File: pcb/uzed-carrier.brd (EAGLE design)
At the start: 51.2 x 43.2 mm, 16 parts

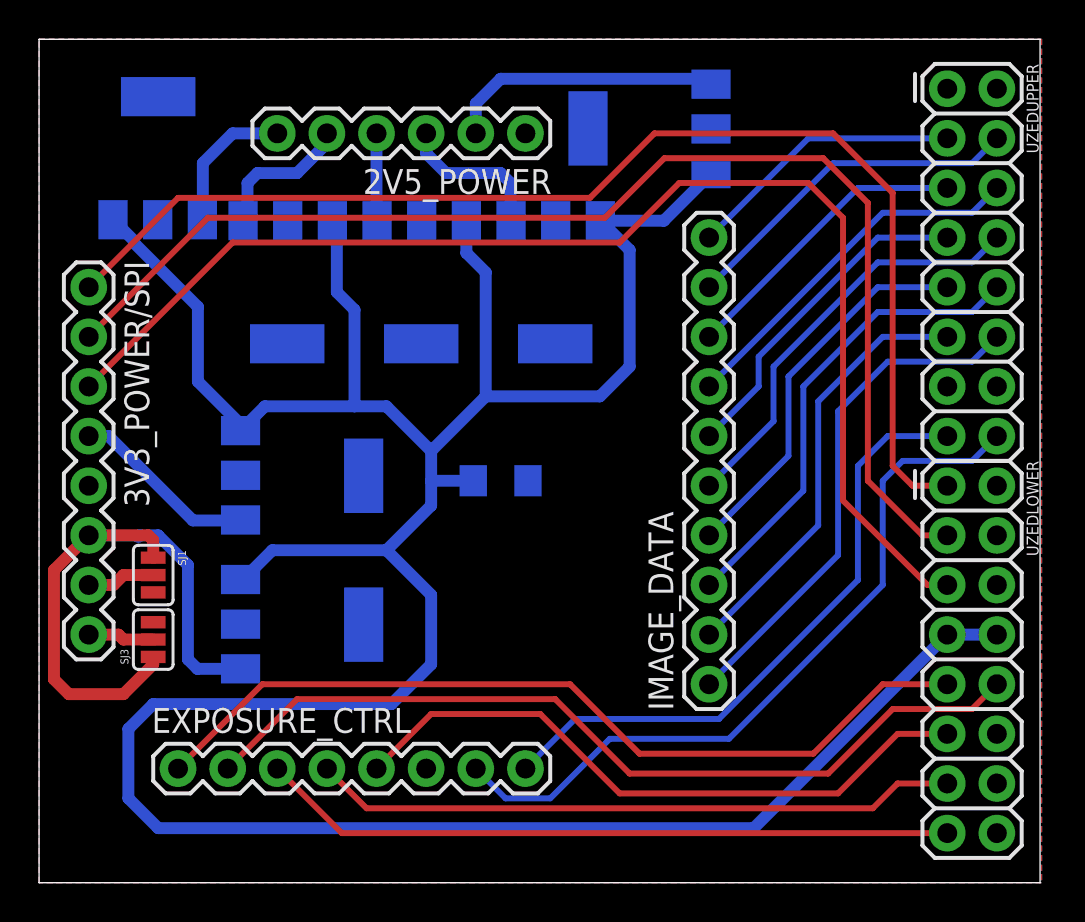
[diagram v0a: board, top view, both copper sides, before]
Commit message: added mosfet for fpga control of board power
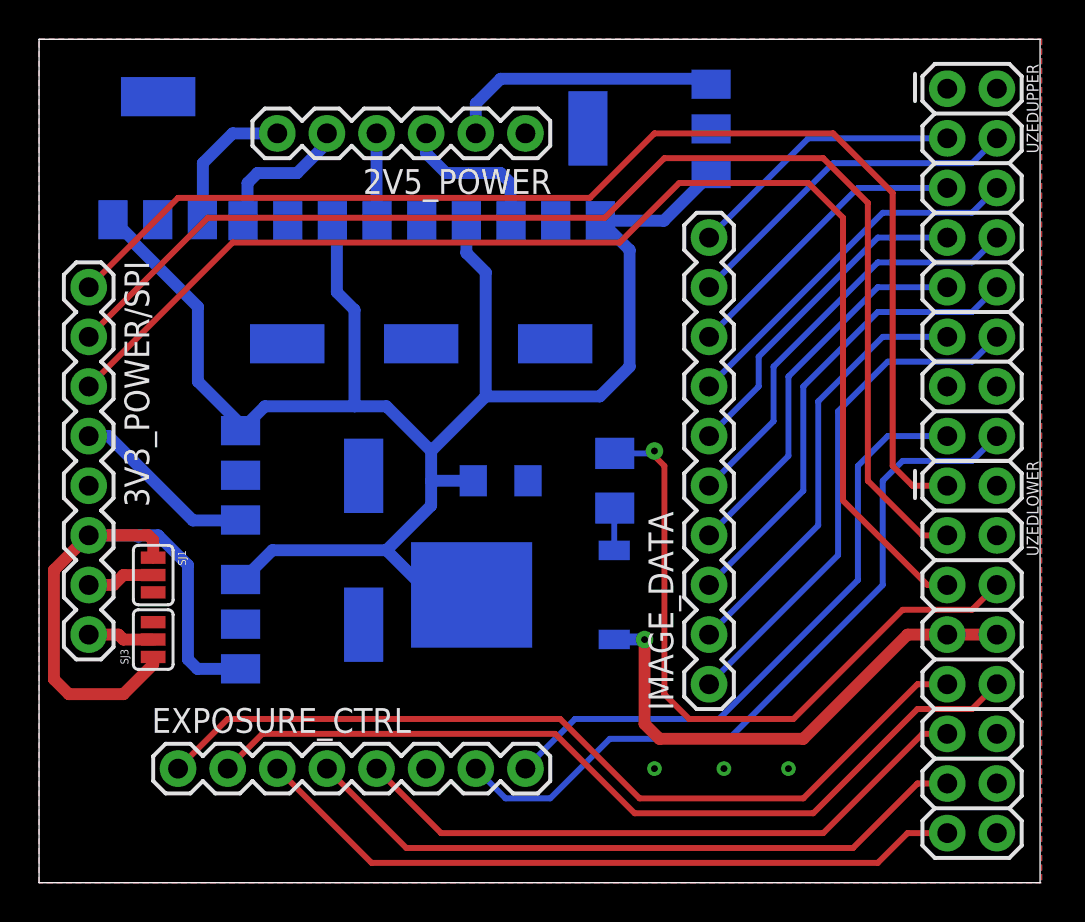
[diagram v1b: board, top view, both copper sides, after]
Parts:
- added Q1: IRFR5305, transistor-power:D-PAK_TO252AA
- added R1: (no value), rcl:M1206
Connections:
- new net FET_GATE: Q1.1, R1.2
- new net N$1: R1.1, UZEDLOWER.6
- new net VRAW: Q1.3, UZEDLOWER.7, UZEDLOWER.8
- net VIN: now also Q1.4; no longer UZEDLOWER.7, UZEDLOWER.8
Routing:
- net VIN: track 163.4 -> 92.4 mm
- net N$1: track 0.00 -> 35.1 mm, vias 0 -> 1
- net VRAW: track 0.00 -> 26.4 mm, vias 0 -> 1
- net FET_GATE: track 0.00 -> 2.17 mm
- net INT_TIME2: track 33.1 -> 34.8 mm
- net INT_TIME3: track 35.7 -> 36.9 mm
- net INT_TIME1: track 33.3 -> 32.7 mm
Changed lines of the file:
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@@
 <attribute name="PROD_ID" value="CAP-00811" x="23.622" y="20.574" size="1.778" layer="28" rot="MR0" display="off"/>
 </element>
+<element name="Q1" library="transistor-power" library_urn="urn:adsk.eagle:library:400" package="D-PAK_TO252AA" package3d_urn="urn:adsk.eagle:package:29503/1" value="IRFR5305" x="24.638" y="14.732" rot="MR270"/>
+<element name="R1" library="rcl" library_urn="urn:adsk.eagle:library:334" package="M1206" package3d_urn="urn:adsk.eagle:package:23566/1" value="" x="29.464" y="20.574" rot="MR270"/>
 </elements>
 <signals>
@@
 <contactref element="SJ3" pad="3"/>
 <contactref element="C1" pad="-"/>
+<via x="31.496" y="5.842" extent="1-16" drill="0.35"/>
+<via x="35.052" y="5.842" extent="1-16" drill="0.35"/>
+<via x="38.354" y="5.842" extent="1-16" drill="0.35"/>
 </signal>
 <signal name="VIN">
@@
 <contactref element="3V3_4" pad="3"/>
 <contactref element="3V3_3" pad="3"/>
-<contactref element="UZEDLOWER" pad="7"/>
-<contactref element="UZEDLOWER" pad="8"/>
-<wire x1="49.022" y1="12.7" x2="46.482" y2="12.7" width="0.6096" layer="16"/>
-<wire x1="46.482" y1="12.7" x2="36.576" y2="2.794" width="0.6096" layer="16"/>
-<wire x1="36.576" y1="2.794" x2="6.096" y2="2.794" width="0.6096" layer="16"/>
-<wire x1="6.096" y1="2.794" x2="4.572" y2="4.318" width="0.6096" layer="16"/>
-<wire x1="4.572" y1="4.318" x2="4.572" y2="7.874" width="0.6096" layer="16"/>
-<wire x1="4.572" y1="7.874" x2="5.842" y2="9.144" width="0.6096" layer="16"/>
-<wire x1="5.842" y1="9.144" x2="18.034" y2="9.144" width="0.6096" layer="16"/>
-<wire x1="18.034" y1="9.144" x2="20.066" y2="11.176" width="0.6096" layer="16"/>
-<wire x1="20.066" y1="14.732" x2="20.066" y2="11.176" width="0.6096" layer="16"/>
-<wire x1="11.938" y1="17.018" x2="17.78" y2="17.018" width="0.6096" layer="16"/>
+<wire x1="17.78" y1="17.018" x2="11.938" y2="17.018" width="0.6096" layer="16"/>
 <wire x1="11.938" y1="17.018" x2="10.4394" y2="15.5194" width="0.6096" layer="16"/>
 <wire x1="10.4394" y1="15.5194" x2="10.3124" y2="15.5194" width="0.6096" layer="16"/>
@@
 <wire x1="8.128" y1="25.654" x2="10.3124" y2="23.4696" width="0.6096" layer="16"/>
 <wire x1="10.3124" y1="23.4696" x2="10.3124" y2="23.1394" width="0.6096" layer="16"/>
-<wire x1="17.78" y1="17.018" x2="20.066" y2="14.732" width="0.6096" layer="16"/>
 <contactref element="C1" pad="+"/>
 <wire x1="22.222" y1="20.574" x2="20.06829375" y2="20.574" width="0.6096" layer="16"/>
 <wire x1="20.06829375" y1="20.574" x2="20.066" y2="20.57629375" width="0.6096" layer="16"/>
+<contactref element="Q1" pad="4"/>
+<wire x1="22.138" y1="14.732" x2="20.066" y2="14.732" width="0.6096" layer="16"/>
+<wire x1="20.066" y1="14.732" x2="17.78" y2="17.018" width="0.6096" layer="16"/>
 </signal>
 <signal name="D0">
@@
 <contactref element="EXPOSURE_CTRL" pad="5"/>
 <contactref element="UZEDLOWER" pad="11"/>
-<wire x1="17.272" y1="5.842" x2="20.066" y2="8.636" width="0.3048" layer="1"/>
-<wire x1="20.066" y1="8.636" x2="25.654" y2="8.636" width="0.3048" layer="1"/>
-<wire x1="25.654" y1="8.636" x2="29.718" y2="4.572" width="0.3048" layer="1"/>
-<wire x1="40.894" y1="4.572" x2="43.942" y2="7.62" width="0.3048" layer="1"/>
-<wire x1="43.942" y1="7.62" x2="46.482" y2="7.62" width="0.3048" layer="1"/>
-<wire x1="29.718" y1="4.572" x2="40.894" y2="4.572" width="0.3048" layer="1"/>
+<wire x1="17.272" y1="5.842" x2="20.574" y2="2.54" width="0.3048" layer="1"/>
+<wire x1="40.132" y1="2.54" x2="45.212" y2="7.62" width="0.3048" layer="1"/>
+<wire x1="45.212" y1="7.62" x2="46.482" y2="7.62" width="0.3048" layer="1"/>
+<wire x1="20.574" y1="2.54" x2="40.132" y2="2.54" width="0.3048" layer="1"/>
 </signal>
 <signal name="INT_TIME2">
 <contactref element="EXPOSURE_CTRL" pad="4"/>
 <contactref element="UZEDLOWER" pad="13"/>
-<wire x1="14.732" y1="5.842" x2="16.764" y2="3.81" width="0.3048" layer="1"/>
-<wire x1="16.764" y1="3.81" x2="42.672" y2="3.81" width="0.3048" layer="1"/>
-<wire x1="42.672" y1="3.81" x2="43.942" y2="5.08" width="0.3048" layer="1"/>
-<wire x1="43.942" y1="5.08" x2="46.482" y2="5.08" width="0.3048" layer="1"/>
+<wire x1="14.732" y1="5.842" x2="18.796" y2="1.778" width="0.3048" layer="1"/>
+<wire x1="18.796" y1="1.778" x2="41.656" y2="1.778" width="0.3048" layer="1"/>
+<wire x1="41.656" y1="1.778" x2="44.958" y2="5.08" width="0.3048" layer="1"/>
+<wire x1="44.958" y1="5.08" x2="46.482" y2="5.08" width="0.3048" layer="1"/>
 </signal>
 <signal name="INT_TIME3">
 <contactref element="EXPOSURE_CTRL" pad="3"/>
 <contactref element="UZEDLOWER" pad="15"/>
-<wire x1="12.192" y1="5.842" x2="15.494" y2="2.54" width="0.3048" layer="1"/>
-<wire x1="15.494" y1="2.54" x2="46.482" y2="2.54" width="0.3048" layer="1"/>
+<wire x1="12.192" y1="5.842" x2="17.018" y2="1.016" width="0.3048" layer="1"/>
+<wire x1="17.018" y1="1.016" x2="42.926" y2="1.016" width="0.3048" layer="1"/>
+<wire x1="42.926" y1="1.016" x2="44.45" y2="2.54" width="0.3048" layer="1"/>
+<wire x1="44.45" y1="2.54" x2="46.482" y2="2.54" width="0.3048" layer="1"/>
 </signal>
 <signal name="FRAME_VALID">
 <contactref element="EXPOSURE_CTRL" pad="2"/>
 <contactref element="UZEDLOWER" pad="10"/>
-<wire x1="9.652" y1="5.842" x2="13.208" y2="9.398" width="0.3048" layer="1"/>
-<wire x1="26.416" y1="9.398" x2="30.226" y2="5.588" width="0.3048" layer="1"/>
-<wire x1="30.226" y1="5.588" x2="40.386" y2="5.588" width="0.3048" layer="1"/>
-<wire x1="40.386" y1="5.588" x2="43.688" y2="8.89" width="0.3048" layer="1"/>
-<wire x1="43.688" y1="8.89" x2="47.752" y2="8.89" width="0.3048" layer="1"/>
+<wire x1="9.652" y1="5.842" x2="11.43" y2="7.62" width="0.3048" layer="1"/>
+<wire x1="26.416" y1="7.62" x2="30.48" y2="3.556" width="0.3048" layer="1"/>
+<wire x1="30.48" y1="3.556" x2="39.624" y2="3.556" width="0.3048" layer="1"/>
+<wire x1="39.624" y1="3.556" x2="44.958" y2="8.89" width="0.3048" layer="1"/>
+<wire x1="44.958" y1="8.89" x2="47.752" y2="8.89" width="0.3048" layer="1"/>
 <wire x1="47.752" y1="8.89" x2="49.022" y2="10.16" width="0.3048" layer="1"/>
-<wire x1="13.208" y1="9.398" x2="26.416" y2="9.398" width="0.3048" layer="1"/>
+<wire x1="11.43" y1="7.62" x2="26.416" y2="7.62" width="0.3048" layer="1"/>
 </signal>
 <signal name="LINE_VALID">
 <contactref element="EXPOSURE_CTRL" pad="1"/>
 <contactref element="UZEDLOWER" pad="9"/>
-<wire x1="7.112" y1="5.842" x2="11.43" y2="10.16" width="0.3048" layer="1"/>
-<wire x1="11.43" y1="10.16" x2="27.178" y2="10.16" width="0.3048" layer="1"/>
-<wire x1="27.178" y1="10.16" x2="30.734" y2="6.604" width="0.3048" layer="1"/>
-<wire x1="30.734" y1="6.604" x2="39.624" y2="6.604" width="0.3048" layer="1"/>
-<wire x1="39.624" y1="6.604" x2="43.18" y2="10.16" width="0.3048" layer="1"/>
-<wire x1="43.18" y1="10.16" x2="46.482" y2="10.16" width="0.3048" layer="1"/>
+<wire x1="7.112" y1="5.842" x2="9.652" y2="8.382" width="0.3048" layer="1"/>
+<wire x1="9.652" y1="8.382" x2="26.67" y2="8.382" width="0.3048" layer="1"/>
+<wire x1="26.67" y1="8.382" x2="30.734" y2="4.318" width="0.3048" layer="1"/>
+<wire x1="30.734" y1="4.318" x2="39.116" y2="4.318" width="0.3048" layer="1"/>
+<wire x1="39.116" y1="4.318" x2="44.958" y2="10.16" width="0.3048" layer="1"/>
+<wire x1="44.958" y1="10.16" x2="46.482" y2="10.16" width="0.3048" layer="1"/>
 </signal>
 <signal name="VPIX">
@@
 <wire x1="44.704" y1="20.32" x2="46.482" y2="20.32" width="0.3048" layer="1"/>
 </signal>
+<signal name="VRAW">
+<contactref element="UZEDLOWER" pad="7"/>
+<contactref element="UZEDLOWER" pad="8"/>
+<contactref element="Q1" pad="3"/>
+<wire x1="29.438" y1="12.452" x2="30.982" y2="12.452" width="0.6096" layer="16"/>
+<wire x1="30.982" y1="12.452" x2="30.988" y2="12.446" width="0.6096" layer="16"/>
+<via x="30.988" y="12.446" extent="1-16" drill="0.35" diameter="0.9"/>
+<wire x1="30.988" y1="12.446" x2="30.988" y2="8.128" width="0.6096" layer="1"/>
+<wire x1="30.988" y1="8.128" x2="31.75" y2="7.366" width="0.6096" layer="1"/>
+<wire x1="31.75" y1="7.366" x2="39.116" y2="7.366" width="0.6096" layer="1"/>
+<wire x1="39.116" y1="7.366" x2="44.45" y2="12.7" width="0.6096" layer="1"/>
+<wire x1="44.45" y1="12.7" x2="46.482" y2="12.7" width="0.6096" layer="1"/>
+<wire x1="46.482" y1="12.7" x2="49.022" y2="12.7" width="0.6096" layer="1"/>
+</signal>
+<signal name="FET_GATE">
+<contactref element="R1" pad="2"/>
+<contactref element="Q1" pad="1"/>
+<wire x1="29.438" y1="17.012" x2="29.438" y2="19.148" width="0.3048" layer="16"/>
+<wire x1="29.438" y1="19.148" x2="29.464" y2="19.174" width="0.3048" layer="16"/>
+</signal>
+<signal name="N$1">
+<contactref element="R1" pad="1"/>
+<contactref element="UZEDLOWER" pad="6"/>
+<wire x1="29.464" y1="21.974" x2="31.372" y2="21.974" width="0.3048" layer="16"/>
+<wire x1="31.372" y1="21.974" x2="31.496" y2="22.098" width="0.3048" layer="16"/>
+<via x="31.496" y="22.098" extent="1-16" drill="0.35" diameter="0.9"/>
+<wire x1="31.496" y1="22.098" x2="31.496" y2="21.844" width="0.3048" layer="1"/>
+<wire x1="31.496" y1="21.844" x2="32.004" y2="21.336" width="0.3048" layer="1"/>
+<wire x1="32.004" y1="21.336" x2="32.004" y2="9.652" width="0.3048" layer="1"/>
+<wire x1="32.004" y1="9.652" x2="33.274" y2="8.382" width="0.3048" layer="1"/>
+<wire x1="33.274" y1="8.382" x2="38.608" y2="8.382" width="0.3048" layer="1"/>
+<wire x1="38.608" y1="8.382" x2="44.196" y2="13.97" width="0.3048" layer="1"/>
+<wire x1="44.196" y1="13.97" x2="47.752" y2="13.97" width="0.3048" layer="1"/>
+<wire x1="47.752" y1="13.97" x2="49.022" y2="15.24" width="0.3048" layer="1"/>
+</signal>
 </signals>
